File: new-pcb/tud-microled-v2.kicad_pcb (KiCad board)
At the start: 2 copper layers, 93 x 93 mm, 192 parts

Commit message: Refactor code structure for improved readability and maintainability
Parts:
- removed BP_R1C1: BP_R1C1, BondPad_DoE
- removed BP_R1C2: BP_R1C2, BondPad_DoE
- removed BP_R1C3: BP_R1C3, BondPad_DoE
- removed BP_R1C4: BP_R1C4, BondPad_DoE
- removed BP_R1C5: BP_R1C5, BondPad_DoE
- removed BP_R1C6: BP_R1C6, BondPad_DoE
- removed BP_R2C1: BP_R2C1, BondPad_DoE
- removed BP_R2C2: BP_R2C2, BondPad_DoE
- removed BP_R2C3: BP_R2C3, BondPad_DoE
- removed BP_R2C4: BP_R2C4, BondPad_DoE
- removed BP_R2C5: BP_R2C5, BondPad_DoE
- removed BP_R2C6: BP_R2C6, BondPad_DoE
- removed BP_R3C1: BP_R3C1, BondPad_DoE
- removed BP_R3C2: BP_R3C2, BondPad_DoE
- removed BP_R3C3: BP_R3C3, BondPad_DoE
- removed BP_R3C4: BP_R3C4, BondPad_DoE
- removed BP_R3C5: BP_R3C5, BondPad_DoE
- removed BP_R3C6: BP_R3C6, BondPad_DoE
- removed BP_R4C1: BP_R4C1, BondPad_DoE
- removed BP_R4C2: BP_R4C2, BondPad_DoE
- removed BP_R4C3: BP_R4C3, BondPad_DoE
- removed BP_R4C4: BP_R4C4, BondPad_DoE
- removed BP_R4C5: BP_R4C5, BondPad_DoE
- removed BP_R4C6: BP_R4C6, BondPad_DoE
- removed BP_R5C1: BP_R5C1, BondPad_DoE
- removed BP_R5C2: BP_R5C2, BondPad_DoE
- removed BP_R5C3: BP_R5C3, BondPad_DoE
- removed BP_R5C4: BP_R5C4, BondPad_DoE
- removed BP_R5C5: BP_R5C5, BondPad_DoE
- removed BP_R5C6: BP_R5C6, BondPad_DoE
- removed BP_R6C1: BP_R6C1, BondPad_DoE
- removed BP_R6C2: BP_R6C2, BondPad_DoE
- removed BP_R6C3: BP_R6C3, BondPad_DoE
- removed BP_R6C4: BP_R6C4, BondPad_DoE
- removed BP_R6C5: BP_R6C5, BondPad_DoE
- removed BP_R6C6: BP_R6C6, BondPad_DoE
- removed FID1: FID1, Fiducial_1mm
- removed FID2: FID2, Fiducial_1mm
- removed FID3: FID3, Fiducial_1mm
- removed FID4: FID4, Fiducial_1mm
- removed H_N_1: H_N_1, Header_2.54mm
- removed H_N_10: H_N_10, Header_2.54mm
- removed H_N_11: H_N_11, Header_2.54mm
- removed H_N_12: H_N_12, Header_2.54mm
- removed H_N_13: H_N_13, Header_2.54mm
- removed H_N_14: H_N_14, Header_2.54mm
- removed H_N_15: H_N_15, Header_2.54mm
- removed H_N_16: H_N_16, Header_2.54mm
- removed H_N_17: H_N_17, Header_2.54mm
- removed H_N_18: H_N_18, Header_2.54mm
- removed H_N_19: H_N_19, Header_2.54mm
- removed H_N_2: H_N_2, Header_2.54mm
- removed H_N_20: H_N_20, Header_2.54mm
- removed H_N_21: H_N_21, Header_2.54mm
- removed H_N_22: H_N_22, Header_2.54mm
- removed H_N_23: H_N_23, Header_2.54mm
- removed H_N_24: H_N_24, Header_2.54mm
- removed H_N_25: H_N_25, Header_2.54mm
- removed H_N_26: H_N_26, Header_2.54mm
- removed H_N_27: H_N_27, Header_2.54mm
- removed H_N_28: H_N_28, Header_2.54mm
- removed H_N_29: H_N_29, Header_2.54mm
- removed H_N_3: H_N_3, Header_2.54mm
- removed H_N_30: H_N_30, Header_2.54mm
- removed H_N_31: H_N_31, Header_2.54mm
- removed H_N_32: H_N_32, Header_2.54mm
- removed H_N_4: H_N_4, Header_2.54mm
- removed H_N_5: H_N_5, Header_2.54mm
- removed H_N_6: H_N_6, Header_2.54mm
- removed H_N_7: H_N_7, Header_2.54mm
- removed H_N_8: H_N_8, Header_2.54mm
- removed H_N_9: H_N_9, Header_2.54mm
- removed H_S_1: H_S_1, Header_2.54mm
- removed H_S_10: H_S_10, Header_2.54mm
- removed H_S_11: H_S_11, Header_2.54mm
- removed H_S_12: H_S_12, Header_2.54mm
- removed H_S_13: H_S_13, Header_2.54mm
- removed H_S_14: H_S_14, Header_2.54mm
- removed H_S_15: H_S_15, Header_2.54mm
- removed H_S_16: H_S_16, Header_2.54mm
- removed H_S_17: H_S_17, Header_2.54mm
- removed H_S_18: H_S_18, Header_2.54mm
- removed H_S_19: H_S_19, Header_2.54mm
- removed H_S_2: H_S_2, Header_2.54mm
- removed H_S_20: H_S_20, Header_2.54mm
- removed H_S_21: H_S_21, Header_2.54mm
- removed H_S_22: H_S_22, Header_2.54mm
- removed H_S_23: H_S_23, Header_2.54mm
- removed H_S_24: H_S_24, Header_2.54mm
- removed H_S_25: H_S_25, Header_2.54mm
- removed H_S_26: H_S_26, Header_2.54mm
- removed H_S_27: H_S_27, Header_2.54mm
- removed H_S_28: H_S_28, Header_2.54mm
- removed H_S_29: H_S_29, Header_2.54mm
- removed H_S_3: H_S_3, Header_2.54mm
- removed H_S_30: H_S_30, Header_2.54mm
- removed H_S_31: H_S_31, Header_2.54mm
- removed H_S_32: H_S_32, Header_2.54mm
- removed H_S_4: H_S_4, Header_2.54mm
- removed H_S_5: H_S_5, Header_2.54mm
- removed H_S_6: H_S_6, Header_2.54mm
- removed H_S_7: H_S_7, Header_2.54mm
- removed H_S_8: H_S_8, Header_2.54mm
- removed H_S_9: H_S_9, Header_2.54mm
- removed PP_D1_A: PP_D1_A, Probe_1.27mm
- removed PP_D1_KB: PP_D1_KB, Probe_1.27mm
- removed PP_D1_KG: PP_D1_KG, Probe_1.27mm
- removed PP_D1_KR: PP_D1_KR, Probe_1.27mm
- removed PP_D2_A: PP_D2_A, Probe_1.27mm
- removed PP_D2_KB: PP_D2_KB, Probe_1.27mm
- removed PP_D2_KG: PP_D2_KG, Probe_1.27mm
- removed PP_D2_KR: PP_D2_KR, Probe_1.27mm
- removed PP_D3_A: PP_D3_A, Probe_1.27mm
- removed PP_D3_KB: PP_D3_KB, Probe_1.27mm
- removed PP_D3_KG: PP_D3_KG, Probe_1.27mm
- removed PP_D3_KR: PP_D3_KR, Probe_1.27mm
- removed PP_D4_A: PP_D4_A, Probe_1.27mm
- removed PP_D4_KB: PP_D4_KB, Probe_1.27mm
- removed PP_D4_KG: PP_D4_KG, Probe_1.27mm
- removed PP_D4_KR: PP_D4_KR, Probe_1.27mm
- removed PP_D5_A: PP_D5_A, Probe_1.27mm
- removed PP_D5_KB: PP_D5_KB, Probe_1.27mm
- removed PP_D5_KG: PP_D5_KG, Probe_1.27mm
- removed PP_D5_KR: PP_D5_KR, Probe_1.27mm
- removed PP_D6_A: PP_D6_A, Probe_1.27mm
- removed PP_D6_KB: PP_D6_KB, Probe_1.27mm
- removed PP_D6_KG: PP_D6_KG, Probe_1.27mm
- removed PP_D6_KR: PP_D6_KR, Probe_1.27mm
- removed PP_D7_A: PP_D7_A, Probe_1.27mm
- removed PP_D7_KB: PP_D7_KB, Probe_1.27mm
- removed PP_D7_KG: PP_D7_KG, Probe_1.27mm
- removed PP_D7_KR: PP_D7_KR, Probe_1.27mm
- removed PP_D8_A: PP_D8_A, Probe_1.27mm
- removed PP_D8_KB: PP_D8_KB, Probe_1.27mm
- removed PP_D8_KG: PP_D8_KG, Probe_1.27mm
- removed PP_D8_KR: PP_D8_KR, Probe_1.27mm
- removed PP_DCL12_IN: PP_DCL12_IN, Probe_1.27mm
- removed PP_DCL12_OUT: PP_DCL12_OUT, Probe_1.27mm
- removed PP_DCL6_IN: PP_DCL6_IN, Probe_1.27mm
- removed PP_DCL6_OUT: PP_DCL6_OUT, Probe_1.27mm
- removed PP_EIS_OPEN_A: PP_EIS_OPEN_A, Probe_1.27mm
- removed PP_EIS_OPEN_B: PP_EIS_OPEN_B, Probe_1.27mm
- removed PP_EIS_SHORT_A: PP_EIS_SHORT_A, Probe_1.27mm
- removed PP_EIS_SHORT_B: PP_EIS_SHORT_B, Probe_1.27mm
- removed PP_GND1: PP_GND1, Probe_1.27mm
- removed PP_GND2: PP_GND2, Probe_1.27mm
- removed PP_NTC1: PP_NTC1, Probe_1.27mm
- removed PP_NTC2: PP_NTC2, Probe_1.27mm
- removed PP_NTC3: PP_NTC3, Probe_1.27mm
- removed PP_NTC4: PP_NTC4, Probe_1.27mm
- removed TC1: TC1, TC_Pad_1mm
- removed TC2: TC2, TC_Pad_1mm
- removed TC3: TC3, TC_Pad_1mm
- removed TC4: TC4, TC_Pad_1mm
- removed TLM_W0.25: TLM_W0.25, TLM
- removed TLM_W0.5: TLM_W0.5, TLM
- removed TLM_W1.0: TLM_W1.0, TLM
- removed VDP_W0.15: VDP_W0.15, VDP
- removed VDP_W0.25: VDP_W0.25, VDP
- removed VDP_W0.5: VDP_W0.5, VDP
- removed VDP_W1.0: VDP_W1.0, VDP
- added H_N: TSW-140-07-G-S, Header_2.54mm, F.Cu at (7.13, 13.5)
- added H_S: TSW-140-07-G-S, Header_2.54mm, F.Cu at (7.13, 85.0)
- D1: value D1 -> WL-SFCC RGB (DNP)
- D2: value D2 -> WL-SFCC RGB (DNP)
- D3: value D3 -> WL-SFCC RGB (DNP)
- D4: value D4 -> WL-SFCC RGB (DNP)
- D5: value D5 -> WL-SFCC RGB (DNP)
- D6: value D6 -> WL-SFCC RGB (DNP)
- D7: value D7 -> WL-SFCC RGB (DNP)
- D8: value D8 -> WL-SFCC RGB (DNP)
- DCL12_L1: value DCL12_L1 -> WL-SFCC RGB (DNP)
- DCL12_L10: value DCL12_L10 -> WL-SFCC RGB (DNP)
- DCL12_L11: value DCL12_L11 -> WL-SFCC RGB (DNP)
- DCL12_L12: value DCL12_L12 -> WL-SFCC RGB (DNP)
- DCL12_L2: value DCL12_L2 -> WL-SFCC RGB (DNP)
- DCL12_L3: value DCL12_L3 -> WL-SFCC RGB (DNP)
- DCL12_L4: value DCL12_L4 -> WL-SFCC RGB (DNP)
- DCL12_L5: value DCL12_L5 -> WL-SFCC RGB (DNP)
- DCL12_L6: value DCL12_L6 -> WL-SFCC RGB (DNP)
- DCL12_L7: value DCL12_L7 -> WL-SFCC RGB (DNP)
- DCL12_L8: value DCL12_L8 -> WL-SFCC RGB (DNP)
- DCL12_L9: value DCL12_L9 -> WL-SFCC RGB (DNP)
- DCL6_L1: value DCL6_L1 -> WL-SFCC RGB (DNP)
- DCL6_L2: value DCL6_L2 -> WL-SFCC RGB (DNP)
- DCL6_L3: value DCL6_L3 -> WL-SFCC RGB (DNP)
- DCL6_L4: value DCL6_L4 -> WL-SFCC RGB (DNP)
- DCL6_L5: value DCL6_L5 -> WL-SFCC RGB (DNP)
- DCL6_L6: value DCL6_L6 -> WL-SFCC RGB (DNP)
- R_EIS_LOAD: value R_EIS_LOAD -> RT0603BRD07100RL
- TH1: value TH1 -> NTCG104BH103HT1
- TH2: value TH2 -> NTCG104BH103HT1
- TH3: value TH3 -> NTCG104BH103HT1
- TH4: value TH4 -> NTCG104BH103HT1

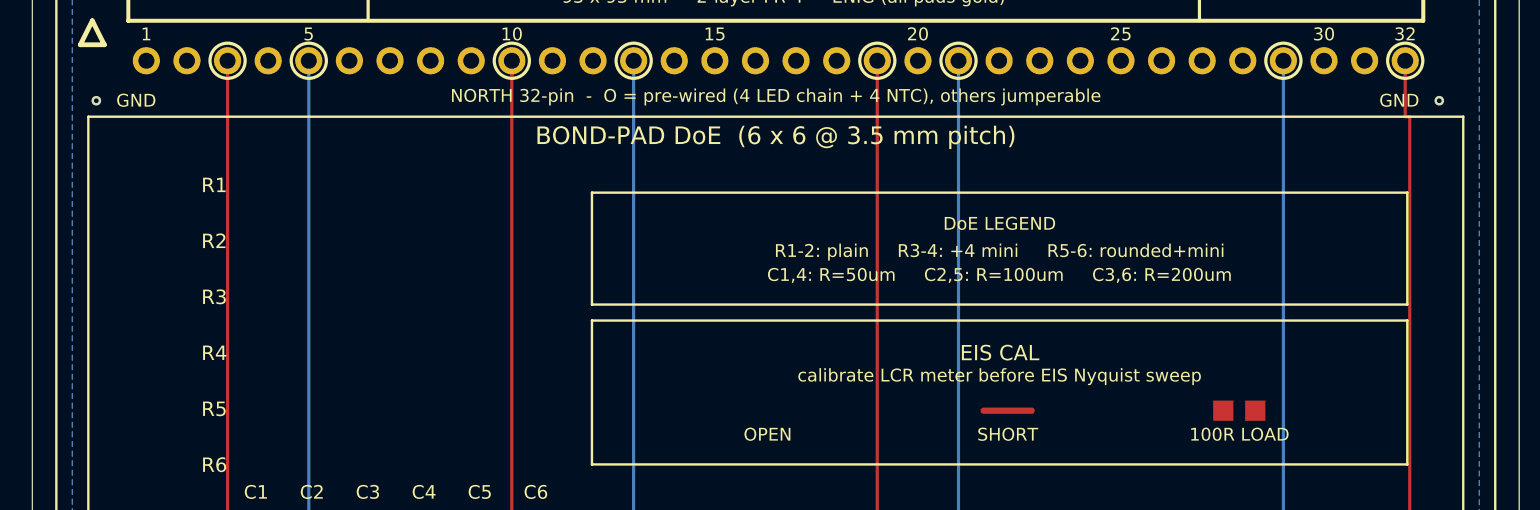
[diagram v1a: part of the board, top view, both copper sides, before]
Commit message: Remove email correspondence and related documents for ET4277/ET4391 project; update KiCad project zip file; fix BOM issues for Eurocircuits; switch to bare PCB order for faster turnaround.
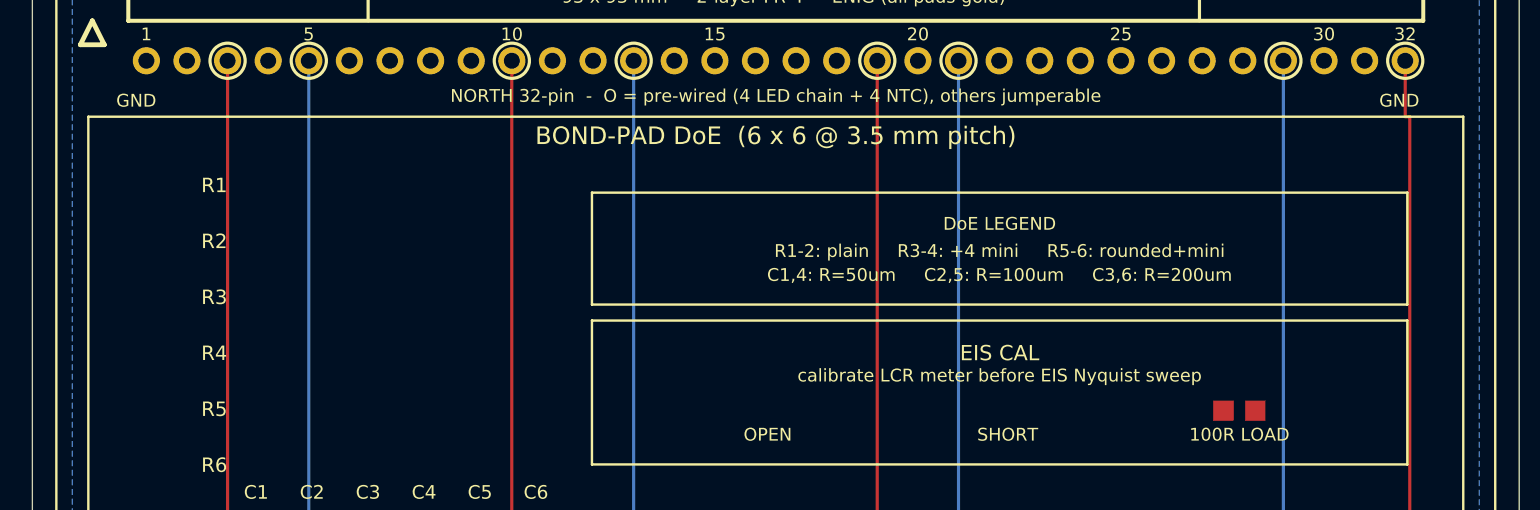
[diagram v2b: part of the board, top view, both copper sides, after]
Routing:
- net EIS_SHORT: track 3.00 -> 0.00 mm
- net GND: vias 6 -> 4

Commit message: Update KiCad project files for microLED design; modified project archive to reflect recent changes.
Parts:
- added BP_R1C1: BP_R1C1, BondPad_DoE, F.Cu at (14.0, 21.0)
- added BP_R1C2: BP_R1C2, BondPad_DoE, F.Cu at (17.5, 21.0)
- added BP_R1C3: BP_R1C3, BondPad_DoE, F.Cu at (21.0, 21.0)
- added BP_R1C4: BP_R1C4, BondPad_DoE, F.Cu at (24.5, 21.0)
- added BP_R1C5: BP_R1C5, BondPad_DoE, F.Cu at (28.0, 21.0)
- added BP_R1C6: BP_R1C6, BondPad_DoE, F.Cu at (31.5, 21.0)
- added BP_R2C1: BP_R2C1, BondPad_DoE, F.Cu at (14.0, 24.5)
- added BP_R2C2: BP_R2C2, BondPad_DoE, F.Cu at (17.5, 24.5)
- added BP_R2C3: BP_R2C3, BondPad_DoE, F.Cu at (21.0, 24.5)
- added BP_R2C4: BP_R2C4, BondPad_DoE, F.Cu at (24.5, 24.5)
- added BP_R2C5: BP_R2C5, BondPad_DoE, F.Cu at (28.0, 24.5)
- added BP_R2C6: BP_R2C6, BondPad_DoE, F.Cu at (31.5, 24.5)
- added BP_R3C1: BP_R3C1, BondPad_DoE, F.Cu at (14.0, 28.0)
- added BP_R3C2: BP_R3C2, BondPad_DoE, F.Cu at (17.5, 28.0)
- added BP_R3C3: BP_R3C3, BondPad_DoE, F.Cu at (21.0, 28.0)
- added BP_R3C4: BP_R3C4, BondPad_DoE, F.Cu at (24.5, 28.0)
- added BP_R3C5: BP_R3C5, BondPad_DoE, F.Cu at (28.0, 28.0)
- added BP_R3C6: BP_R3C6, BondPad_DoE, F.Cu at (31.5, 28.0)
- added BP_R4C1: BP_R4C1, BondPad_DoE, F.Cu at (14.0, 31.5)
- added BP_R4C2: BP_R4C2, BondPad_DoE, F.Cu at (17.5, 31.5)
- added BP_R4C3: BP_R4C3, BondPad_DoE, F.Cu at (21.0, 31.5)
- added BP_R4C4: BP_R4C4, BondPad_DoE, F.Cu at (24.5, 31.5)
- added BP_R4C5: BP_R4C5, BondPad_DoE, F.Cu at (28.0, 31.5)
- added BP_R4C6: BP_R4C6, BondPad_DoE, F.Cu at (31.5, 31.5)
- added BP_R5C1: BP_R5C1, BondPad_DoE, F.Cu at (14.0, 35.0)
- added BP_R5C2: BP_R5C2, BondPad_DoE, F.Cu at (17.5, 35.0)
- added BP_R5C3: BP_R5C3, BondPad_DoE, F.Cu at (21.0, 35.0)
- added BP_R5C4: BP_R5C4, BondPad_DoE, F.Cu at (24.5, 35.0)
- added BP_R5C5: BP_R5C5, BondPad_DoE, F.Cu at (28.0, 35.0)
- added BP_R5C6: BP_R5C6, BondPad_DoE, F.Cu at (31.5, 35.0)
- added BP_R6C1: BP_R6C1, BondPad_DoE, F.Cu at (14.0, 38.5)
- added BP_R6C2: BP_R6C2, BondPad_DoE, F.Cu at (17.5, 38.5)
- added BP_R6C3: BP_R6C3, BondPad_DoE, F.Cu at (21.0, 38.5)
- added BP_R6C4: BP_R6C4, BondPad_DoE, F.Cu at (24.5, 38.5)
- added BP_R6C5: BP_R6C5, BondPad_DoE, F.Cu at (28.0, 38.5)
- added BP_R6C6: BP_R6C6, BondPad_DoE, F.Cu at (31.5, 38.5)
- added FID1: FID1, Fiducial_1mm, F.Cu at (4.00, 4.00)
- added FID2: FID2, Fiducial_1mm, F.Cu at (89.0, 4.00)
- added FID3: FID3, Fiducial_1mm, F.Cu at (4.00, 89.0)
- added FID4: FID4, Fiducial_1mm, F.Cu at (89.0, 89.0)
- added PP_D1_A: PP_D1_A, Probe_1.27mm, F.Cu at (8.50, 81.0)
- added PP_D1_KB: PP_D1_KB, Probe_1.27mm, F.Cu at (12.5, 81.0)
- added PP_D1_KG: PP_D1_KG, Probe_1.27mm, F.Cu at (10.5, 81.0)
- added PP_D1_KR: PP_D1_KR, Probe_1.27mm, F.Cu at (14.5, 81.0)
- added PP_D2_A: PP_D2_A, Probe_1.27mm, F.Cu at (18.5, 81.0)
- added PP_D2_KB: PP_D2_KB, Probe_1.27mm, F.Cu at (22.5, 81.0)
- added PP_D2_KG: PP_D2_KG, Probe_1.27mm, F.Cu at (20.5, 81.0)
- added PP_D2_KR: PP_D2_KR, Probe_1.27mm, F.Cu at (24.5, 81.0)
- added PP_D3_A: PP_D3_A, Probe_1.27mm, F.Cu at (28.5, 81.0)
- added PP_D3_KB: PP_D3_KB, Probe_1.27mm, F.Cu at (32.5, 81.0)
- added PP_D3_KG: PP_D3_KG, Probe_1.27mm, F.Cu at (30.5, 81.0)
- added PP_D3_KR: PP_D3_KR, Probe_1.27mm, F.Cu at (34.5, 81.0)
- added PP_D4_A: PP_D4_A, Probe_1.27mm, F.Cu at (38.5, 81.0)
- added PP_D4_KB: PP_D4_KB, Probe_1.27mm, F.Cu at (42.5, 81.0)
- added PP_D4_KG: PP_D4_KG, Probe_1.27mm, F.Cu at (40.5, 81.0)
- added PP_D4_KR: PP_D4_KR, Probe_1.27mm, F.Cu at (44.5, 81.0)
- added PP_D5_A: PP_D5_A, Probe_1.27mm, F.Cu at (48.5, 81.0)
- added PP_D5_KB: PP_D5_KB, Probe_1.27mm, F.Cu at (52.5, 81.0)
- added PP_D5_KG: PP_D5_KG, Probe_1.27mm, F.Cu at (50.5, 81.0)
- added PP_D5_KR: PP_D5_KR, Probe_1.27mm, F.Cu at (54.5, 81.0)
- added PP_D6_A: PP_D6_A, Probe_1.27mm, F.Cu at (58.5, 81.0)
- added PP_D6_KB: PP_D6_KB, Probe_1.27mm, F.Cu at (62.5, 81.0)
- added PP_D6_KG: PP_D6_KG, Probe_1.27mm, F.Cu at (60.5, 81.0)
- added PP_D6_KR: PP_D6_KR, Probe_1.27mm, F.Cu at (64.5, 81.0)
- added PP_D7_A: PP_D7_A, Probe_1.27mm, F.Cu at (68.5, 81.0)
- added PP_D7_KB: PP_D7_KB, Probe_1.27mm, F.Cu at (72.5, 81.0)
- added PP_D7_KG: PP_D7_KG, Probe_1.27mm, F.Cu at (70.5, 81.0)
- added PP_D7_KR: PP_D7_KR, Probe_1.27mm, F.Cu at (74.5, 81.0)
- added PP_D8_A: PP_D8_A, Probe_1.27mm, F.Cu at (78.5, 81.0)
- added PP_D8_KB: PP_D8_KB, Probe_1.27mm, F.Cu at (82.5, 81.0)
- added PP_D8_KG: PP_D8_KG, Probe_1.27mm, F.Cu at (80.5, 81.0)
- added PP_D8_KR: PP_D8_KR, Probe_1.27mm, F.Cu at (84.5, 81.0)
- added PP_DCL12_IN: PP_DCL12_IN, Probe_1.27mm, F.Cu at (53.9, 72.0)
- added PP_DCL12_OUT: PP_DCL12_OUT, Probe_1.27mm, F.Cu at (86.2, 72.0)
- added PP_DCL6_IN: PP_DCL6_IN, Probe_1.27mm, F.Cu at (13.3, 72.0)
- added PP_DCL6_OUT: PP_DCL6_OUT, Probe_1.27mm, F.Cu at (30.6, 72.0)
- added PP_EIS_OPEN_A: PP_EIS_OPEN_A, Probe_1.27mm, F.Cu at (44.5, 35.4)
- added PP_EIS_OPEN_B: PP_EIS_OPEN_B, Probe_1.27mm, F.Cu at (47.5, 35.4)
- added PP_EIS_SHORT_A: PP_EIS_SHORT_A, Probe_1.27mm, F.Cu at (59.5, 35.4)
- added PP_EIS_SHORT_B: PP_EIS_SHORT_B, Probe_1.27mm, F.Cu at (62.5, 35.4)
- added PP_GND1: PP_GND1, Probe_1.27mm, F.Cu at (4.00, 16.0)
- added PP_GND2: PP_GND2, Probe_1.27mm, F.Cu at (88.0, 16.0)
- added PP_NTC1: PP_NTC1, Probe_1.27mm, F.Cu at (15.2, 76.8)
- added PP_NTC2: PP_NTC2, Probe_1.27mm, F.Cu at (35.2, 76.8)
- added PP_NTC3: PP_NTC3, Probe_1.27mm, F.Cu at (55.2, 76.8)
- added PP_NTC4: PP_NTC4, Probe_1.27mm, F.Cu at (75.2, 76.8)
- added TC1: TC1, TC_Pad_1mm, F.Cu at (2.50, 50.5)
- added TC2: TC2, TC_Pad_1mm, F.Cu at (2.50, 64.5)
- added TC3: TC3, TC_Pad_1mm, F.Cu at (90.5, 50.5)
- added TC4: TC4, TC_Pad_1mm, F.Cu at (90.5, 64.5)
- added TLM_W0.25: TLM_W0.25, TLM, F.Cu at (22.0, 50.5)
- added TLM_W0.5: TLM_W0.5, TLM, F.Cu at (50.0, 50.5)
- added TLM_W1.0: TLM_W1.0, TLM, F.Cu at (78.0, 50.5)
- added VDP_W0.15: VDP_W0.15, VDP, F.Cu at (83.0, 61.5)
- added VDP_W0.25: VDP_W0.25, VDP, F.Cu at (62.0, 61.5)
- added VDP_W0.5: VDP_W0.5, VDP, F.Cu at (38.0, 61.5)
- added VDP_W1.0: VDP_W1.0, VDP, F.Cu at (15.0, 61.5)
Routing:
- net EIS_SHORT: track 0.00 -> 3.00 mm
- net GND: vias 4 -> 6
